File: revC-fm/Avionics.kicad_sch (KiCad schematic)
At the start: 45 parts, among them Q32 MMBT4403WT1G, SW1 KMR231NG LFS, U11 ATSAMD51N20A-AUT, U12 MR25H40MDF, U13 MAX706RESA, U4 imu-stamp-revA, Y1 32.768kHz

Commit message: working revC
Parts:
- removed D1: WS2812B, LED_SMD:LED_WS2812B_PLCC4_5.0x5.0mm_P3.2mm, symbol mainboard-rescue:WS2812B-LED-mainboard-rescue
- removed R27: R_US, Resistor_SMD:R_0603_1608Metric, symbol Device:R_US
- added C5, C6, C7: 0.1uF, Capacitor_SMD:C_0603_1608Metric, symbol Device:C
- added D1, D10, D11, D12: SK6812-EC321F, mainboard-SLI:SK6812-EC3210F, symbol mainboard_SLI:SK6812-EC321F
- R25: value R_US -> 976k
- R26: value R_US -> 102k
- R44, R46: value 4.7k -> 2.7k
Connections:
- net 3.3V: now also C5.1, C6.1, C7.1, D1.4 (VDD), D10.4 (VDD), D11.4 (VDD), D12.4 (VDD)
- net GND: now also R26.2, U4.8 (XORL1), C5.2, C6.2, C7.2, D1.1 (VSS), D10.1 (VSS), D11.1 (VSS), D12.1 (VSS)
- net NeoPixel_Out: now also D12.2 (DOUT)
- net at U11.71 (PA21): now also D1.3 (DIN)
- net AIN10 renamed BATT_NTC
- new net: D11.2 (DOUT), D12.3 (DIN)
- new net: D10.2 (DOUT), D11.3 (DIN)
- new net: D1.2 (DOUT), D10.3 (DIN)
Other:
- note added: "XOR1 = 0x0 XOR2 = 0x1"
- note added: "gyros @ 0x68, 0x69 accels @ ox4C, 0x4D mags @ 0x30, 0x31"
- note removed: "TODO: CALCULATE XOR VALUE RESISTORS FOR I2C"
- note removed: "renamed"
- moved on the sheet: C19, C20, C21, C22, C23, C24, C25, C26, C27, C28, C29, C30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

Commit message: working revC
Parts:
- added R16: 1k, Resistor_SMD:R_0603_1608Metric, symbol Device:R_US
- renumbered C31 to C10, C32 to C11, C33 to C12, C34 to C13, C36 to C14, C37 to C15, C20 to C16, C26 to C17, C28 to C18, C21 to C19, C22 to C20, C4 to C21, C5 to C22, C19 to C23, C7 to C24, C6 to C25, C35 to C26, C23 to C4, C24 to C5, C25 to C6, C27 to C7, C29 to C8, C30 to C9, D10 to D1, D1 to D2, D12 to D3, D11 to D4, R41 to R10, R51 to R11, R42 to R12, R43 to R13, R25 to R14, R5 to R15, R26 to R17, R24 to R18, R48 to R19, R50 to R20, R46 to R21, R44 to R22, R45 to R23, R47 to R8, R49 to R9, U13 to U4, U4 to U5, U11 to U6, U12 to U7
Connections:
- net at Q32.3 (C), R18.1: now also R16.1; no longer U5.5 (EN)
- new net: R16.2, U5.5 (EN)
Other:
- moved on the sheet: C21, Q32, R14, R15, R17, R18, U5

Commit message: working revC
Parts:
- removed Q32: MMBT4403WT1G, Package_TO_SOT_SMD:SOT-323_SC-70, symbol mainboard-rescue:Q_PNP_BEC-Device-mainboard-rescue
- removed R18: 10Meg, Resistor_SMD:R_0603_1608Metric, symbol Device:R_US
- added C98: 0.1uF, Capacitor_SMD:C_0603_1608Metric, symbol Device:C
- added R16, R20, R21: 1k, Resistor_SMD:R_0603_1608Metric, symbol Device:R_US
- added R26: 470k, Resistor_SMD:R_0603_1608Metric, symbol Device:R_US
- added R27: 39k, Resistor_SMD:R_0603_1608Metric, symbol Device:R_US
- D1, D2, D3, D4: value SK6812-EC321F -> SK68xx-EC3210x; footprint mainboard-SLI:SK6812-EC3210F -> SierraLobo:SK68xx-EC3210x; symbol mainboard_SLI:SK6812-EC321F -> SierraLobo:SK68xx-EC3210x
- R15: value 1Meg -> 1k
- R25: renamed from R23; value 100k -> 10k
- SW1: footprint mainboard:BTN_KMR2_4.6X2.8 -> SierraLobo:KMR2_4.6X2.8; symbol mainboard:SWITCH_SMT4.6X2.8 -> Switch:SW_SPST; Flight KMR231NG LFS -> (none); Manufacturer_Name C&K -> (none); Manufacturer_Part_Number KMR231NG LFS -> (none); Proto KMR231NG LFS -> (none)
- U4: value MAX706RESA -> MAX708RESA-T; symbol mainboard:MAX708RESA-T -> SierraLobo:MAX708RESA-T; Flight MAX706RESA -> (none); Manufacturer_Name Maxim Integrated -> (none); Manufacturer_Part_Number MAX706RESA -> (none); Proto MAX706RESA -> (none)
- U5: footprint mainboard-SLI:imu-stamp-revA-SMD -> SierraLobo:imu-stamp-revA-SMD; symbol FP-Interface-Card:imu-stamp-revA -> SierraLobo:imu-stamp-revA
- U6: symbol mainboard_SLI:ATSAMD51N20A-AUT -> SierraLobo:ATSAMD51N20A-AUT; MANUFACTURER Microchip -> (none); STANDARD IPC-7351B -> (none)
- U7: footprint mainboard:SON127P600X500X90-9N -> SierraLobo:SON127P600X500X90-9N; symbol mainboard:MR25H40MDF -> SierraLobo:MR25H40MDF; Flight MR25H40MDF -> (none); Manufacturer_Name Everspin Technologies Inc. -> (none); Manufacturer_Part_Number W25Q80DVSNIG -> (none); Proto W25Q80DVSNIG -> (none)
- Y1: Flight ABS07-32.768KHZ-T -> (none); Manufacturer_Name Abracon LLC -> (none); Manufacturer_Part_Number SC-32S32.768kHz20PPM7pF -> (none); Proto SC-32S32.768kHz20PPM7pF -> (none)
- renumbered R16 to R17, R17 to R18, R20 to R22, R21 to R23, R22 to R24
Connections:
- net +3V3 is gone; now on net 3.3V: C21.1, U5.1 (VCC)
- net ~{IMU_EN} is gone; now on an unnamed net: R15.1
- net GND: now also SW1.2 (B), C98.2, R27.1; no longer SW1.B (S), SW1.B' (S1)
- net VPYLD_PG: now reaches U6.13 (PB06)
- net VPYLD_EN: now reaches U6.14 (PB07)
- net VRF_PG: now reaches U6.36 (PB14)
- net VRF_EN: now reaches U6.37 (PB15)
- net at U6.71 (PA21): now also R16.2; no longer D2.3 (DIN)
- net at D4.2 (DOUT): now also R20.2; no longer D3.3 (DIN)
- net at D4.3 (DIN): now also R21.1; no longer D1.2 (DOUT)
- net at D1.3 (DIN): no longer D2.2 (DOUT)
- net IMU_EN: now reaches R17.1
- net at R15.2: now also D2.2 (DOUT)
- net AIN7 renamed SOLAR
- net SOLAR: now also C98.1, R26.2, R27.2
- net ~{IMU_RST}: no longer names the net of U6.83 (PC25)
- new net: R10.1, SW1.1 (A)
- new net: D1.2 (DOUT), R21.2
- new net: D3.3 (DIN), R20.1
- new net: D2.3 (DIN), R16.1
- new net VSOLAR: R26.1
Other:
- moved on the sheet: C10, C11, C12, C13, C14, C15, C16, C17, C18, C19, C20, C21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

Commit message: routing fm
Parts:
- added U36: 74HC595PW,118, Package_SO:TSSOP-16_4.4x5mm_P0.65mm, symbol SierraLobo:74HC595PW,118
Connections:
- net ~{LED_EN} is gone; now on net MUX_S0: U6.79 (PB23)
- net 3.3V: no longer C22.1, C23.1, C24.1, C25.1, D1.4 (VDD), D2.4 (VDD), D3.4 (VDD), D4.4 (VDD)
- net DAC0: no longer U6.7 (PA02)
- net ENAB_GPS: now also U6.72 (PA22); no longer U6.98 (PB01)
- net MUX_S0: no longer U6.72 (PA22)
- net RF1_CS: now also U6.98 (PB01); no longer U6.68 (PB20)
- net SD_CS: now also U6.49 (PA15); no longer U6.87 (PA27)
- net CHRG_SHDN: now reaches U6.16 (PB09)
- net PC20: now reaches U6.60 (PC20)
- net RF2_IO4: now reaches U6.61 (PC21)
- net RF2_RST: now reaches U6.82 (PC24)
- net RF2_IO0: now reaches U6.83 (PC25)
- net AIN11 renamed PC01
- net AIN4 renamed PC02
- net AIN5 renamed AMUX
- net EN_PAYLOAD renamed ENAB_RF2
- net EN_RF renamed ENAB_RF1
- net NeoPixel_Out renamed LED_OUT
- net ~{CHRG_SHDN} renamed PB21
- net ~{CHRG} renamed CHRG_STAT
- net ~{MUX_EN} renamed ~{MUX_EN1}
- new net LED_PWR: C22.1, C23.1, C24.1, C25.1, D1.4 (VDD), D2.4 (VDD), D3.4 (VDD), D4.4 (VDD)
- new net PA02: U6.7 (PA02)
- new net PA27: U6.87 (PA27)
- new net RF2_CS: U6.68 (PB20)
- no-connect marks 4 -> 1
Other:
- added sheet Temp Sensor 8 (temp_senkicad_sch.kicad_sch)
- note added: "Can also be Analog inputs"
- note added: "Place by IMU"
- moved on the sheet: C21, R14, R17, R18, U5

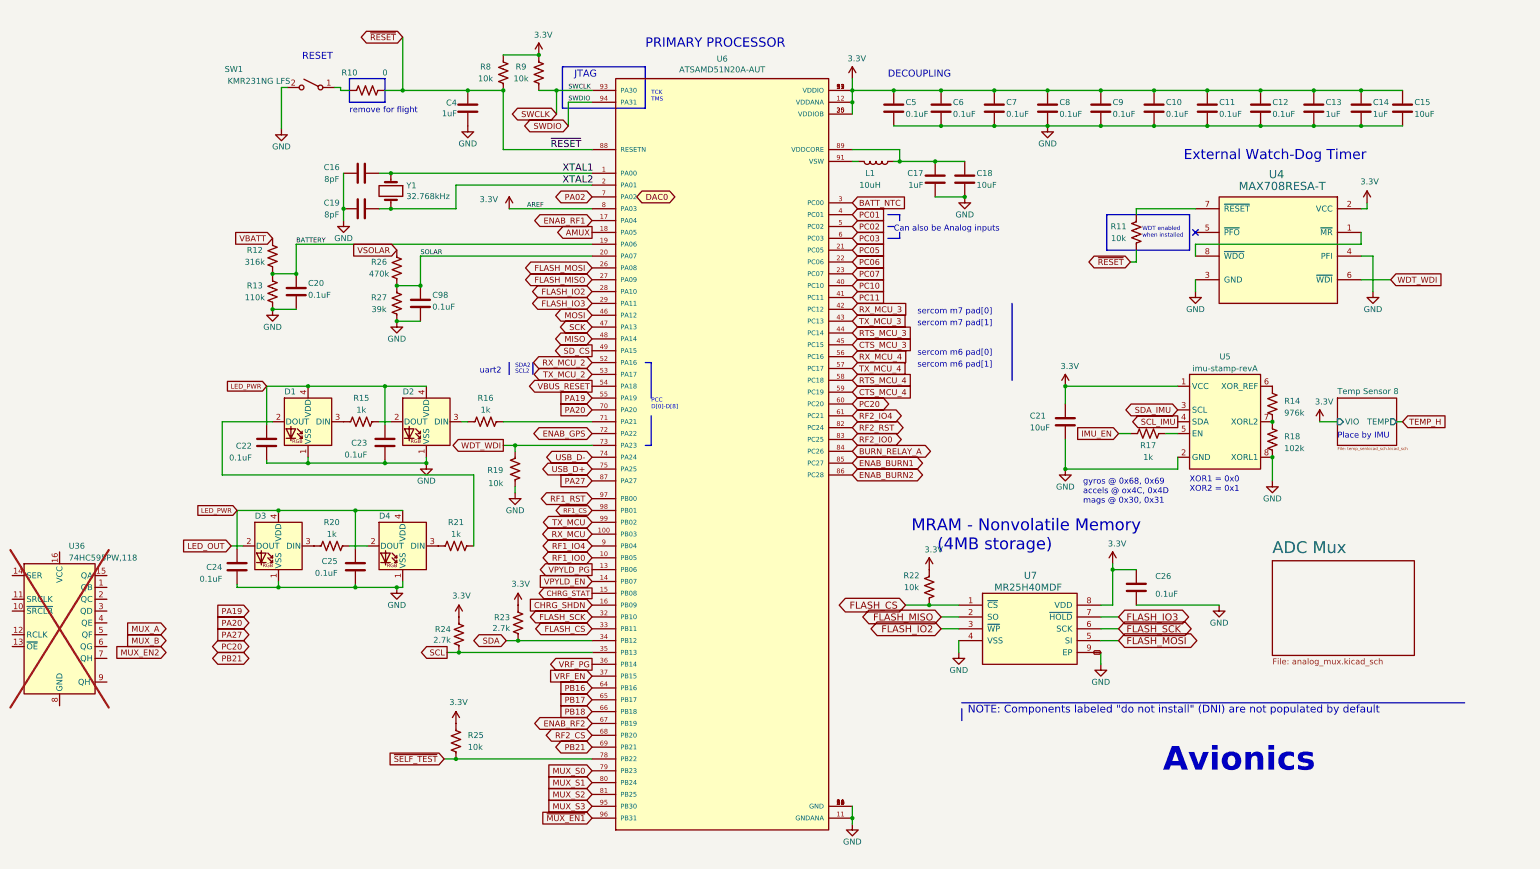
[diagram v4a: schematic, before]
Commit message: updated analog , solar comp, layout
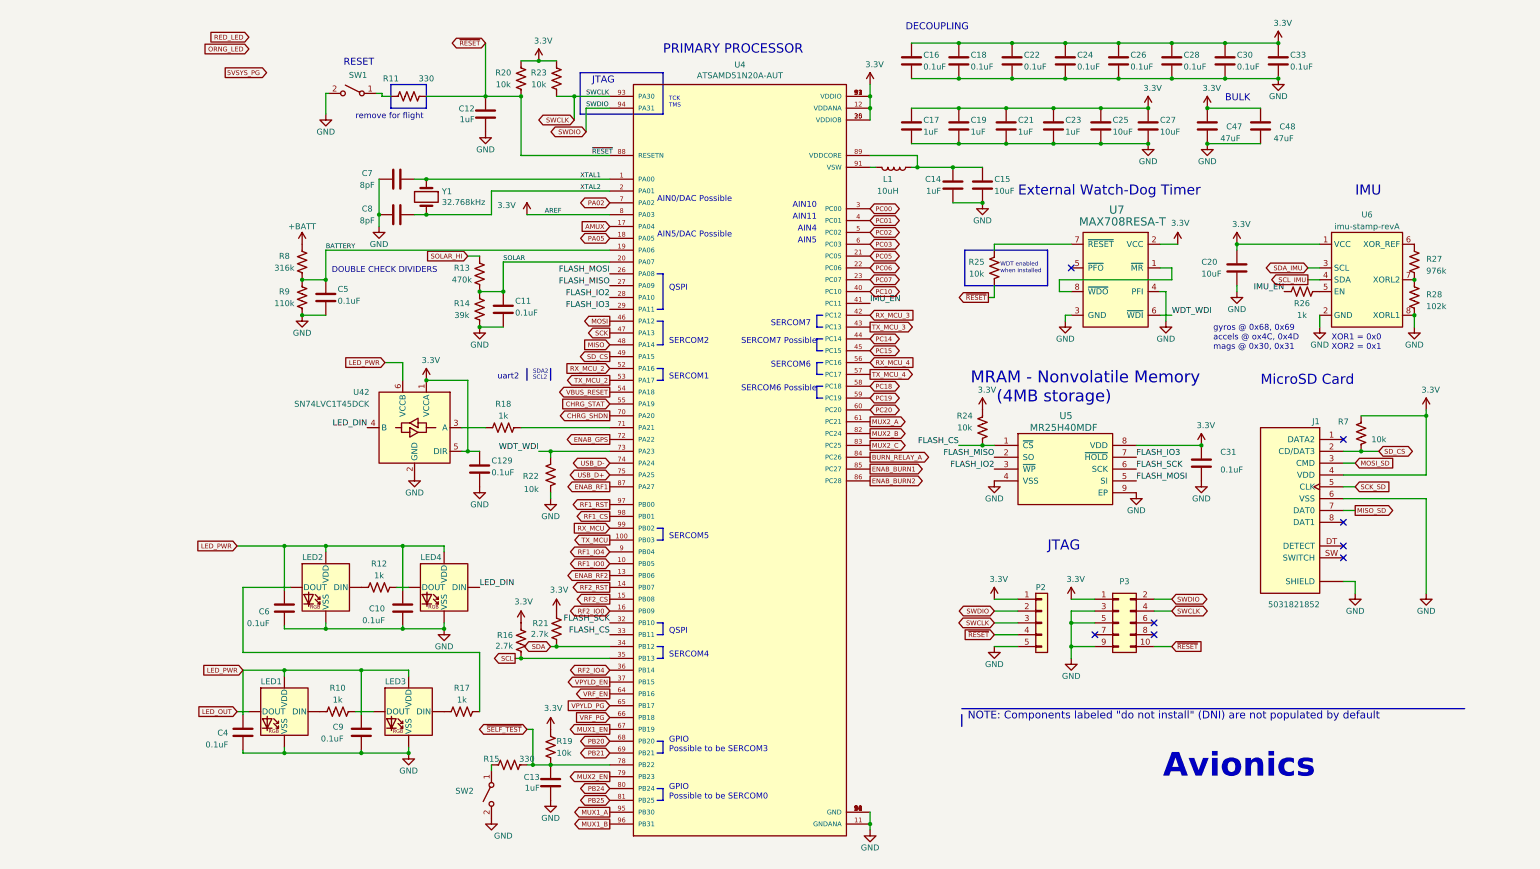
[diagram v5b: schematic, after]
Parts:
- removed U36: 74HC595PW,118, Package_SO:TSSOP-16_4.4x5mm_P0.65mm, symbol SierraLobo:74HC595PW,118
- added C129: 0.1uF, Capacitor_SMD:C_0402_1005Metric, symbol Device:C
- added C13, C21, C23: 1uF, Capacitor_SMD:C_0603_1608Metric, symbol Device:C
- added C27: 10uF, Capacitor_SMD:C_0805_2012Metric, symbol Device:C
- added C47, C48: 47uF, Capacitor_SMD:C_1206_3216Metric, symbol Device:C
- added J1: 5031821852, SierraLobo:MOLEX_503182-1852, symbol SierraLobo:503182-1852
- added P2: TSM-105-01-F-SV, Connector_PinHeader_2.54mm:PinHeader_1x05_P2.54mm_Vertical_SMD_Pin1Right, symbol Connector_Generic:Conn_01x05
- added P3: FTSH-105-01-F-DV-K-TR, Connector_PinHeader_1.27mm:PinHeader_2x05_P1.27mm_Vertical_SMD, symbol Connector_Generic:Conn_02x05_Odd_Even
- added R15: 330, Resistor_SMD:R_0603_1608Metric, symbol Device:R_US
- added R7: 10k, Resistor_SMD:R_0603_1608Metric, symbol Device:R_US
- added SW2: KMR231NG LFS, SierraLobo:KMR2_4.6X2.8, symbol Switch:SW_SPST
- added U42: SN74LVC1T45DCK, Package_TO_SOT_SMD:SOT-363_SC-70-6, symbol Logic_LevelTranslator:SN74LVC1T45DCK
- C10: renamed from C23; footprint Capacitor_SMD:C_0603_1608Metric -> Capacitor_SMD:C_0402_1005Metric
- C11: renamed from C98; footprint Capacitor_SMD:C_0603_1608Metric -> Capacitor_SMD:C_0402_1005Metric
- C16: renamed from C5; footprint Capacitor_SMD:C_0603_1608Metric -> Capacitor_SMD:C_0402_1005Metric
- C18: renamed from C6; footprint Capacitor_SMD:C_0603_1608Metric -> Capacitor_SMD:C_0402_1005Metric
- C22: renamed from C7; footprint Capacitor_SMD:C_0603_1608Metric -> Capacitor_SMD:C_0402_1005Metric
- C24: renamed from C8; footprint Capacitor_SMD:C_0603_1608Metric -> Capacitor_SMD:C_0402_1005Metric
- C26: renamed from C9; footprint Capacitor_SMD:C_0603_1608Metric -> Capacitor_SMD:C_0402_1005Metric
- C28: renamed from C10; footprint Capacitor_SMD:C_0603_1608Metric -> Capacitor_SMD:C_0402_1005Metric
- C30: renamed from C11; footprint Capacitor_SMD:C_0603_1608Metric -> Capacitor_SMD:C_0402_1005Metric
- C31: renamed from C26; footprint Capacitor_SMD:C_0603_1608Metric -> Capacitor_SMD:C_0402_1005Metric
- C33: renamed from C12; footprint Capacitor_SMD:C_0603_1608Metric -> Capacitor_SMD:C_0402_1005Metric
- C4: renamed from C24; footprint Capacitor_SMD:C_0603_1608Metric -> Capacitor_SMD:C_0402_1005Metric
- C5: renamed from C20; footprint Capacitor_SMD:C_0603_1608Metric -> Capacitor_SMD:C_0402_1005Metric
- C6: renamed from C22; footprint Capacitor_SMD:C_0603_1608Metric -> Capacitor_SMD:C_0402_1005Metric
- C7: renamed from C16; footprint Capacitor_SMD:C_0603_1608Metric -> Capacitor_SMD:C_0402_1005Metric
- C8: renamed from C19; footprint Capacitor_SMD:C_0603_1608Metric -> Capacitor_SMD:C_0402_1005Metric
- C9: renamed from C25; footprint Capacitor_SMD:C_0603_1608Metric -> Capacitor_SMD:C_0402_1005Metric
- R11: renamed from R10; value 0 -> 330
- renumbered C4 to C12, C17 to C14, C18 to C15, C13 to C17, C14 to C19, C21 to C20, C15 to C25, D3 to LED1, D1 to LED2, D4 to LED3, D2 to LED4, R20 to R10, R15 to R12, R26 to R13, R27 to R14, R24 to R16, R21 to R17, R16 to R18, R25 to R19, R8 to R20, R23 to R21, R19 to R22, R9 to R23, R22 to R24, R11 to R25, R17 to R26, R14 to R27, R18 to R28, R12 to R8, R13 to R9, U6 to U4, U7 to U5, U5 to U6, U4 to U7
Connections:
- net PA19 is gone; now on net CHRG_STAT: U4.55 (PA19)
- net PA20 is gone; now on net CHRG_SHDN: U4.70 (PA20)
- net PA27 is gone; now on net ENAB_RF1: U4.87 (PA27)
- net PB16 is gone; now on net VRF_EN: U4.64 (PB16)
- net PB17 is gone; now on net VPYLD_PG: U4.65 (PB17)
- net PB18 is gone; now on net VRF_PG: U4.66 (PB18)
- net PC11 is gone; now on net IMU_EN: U4.41 (PC11)
- net 3.3V: now also C129.1, C21.1, C23.1, C27.1, C47.1, C48.1, J1.4 (VDD), P2.1 (Pin_1), P3.1 (Pin_1), R7.2, U42.1 (VCCA), U42.5 (DIR)
- net AMUX: now also U4.17 (PA04); no longer U4.18 (PA05)
- net CHRG_SHDN: no longer U4.16 (PB09)
- net CHRG_STAT: no longer U4.15 (PB08)
- net ENAB_RF1: no longer U4.17 (PA04)
- net ENAB_RF2: now also U4.13 (PB06); no longer U4.67 (PB19)
- net GND: now also C129.2, C13.1, C21.2, C23.2, C27.2, C47.2, C48.2, J1.6 (VSS), J1.P1 (SHIELD), J1.P2 (SHIELD), J1.P3 (SHIELD), J1.P4 (SHIELD), J1.P5 (SHIELD), P2.5 (Pin_5), P3.3 (Pin_3), P3.5 (Pin_5), P3.9 (Pin_9), SW2.2 (B), U42.2 (GND)
- net LED_PWR: now also U42.6 (VCCB)
- net RF2_CS: now also U4.15 (PB08); no longer U4.68 (PB20)
- net RF2_IO0: now also U4.16 (PB09); no longer U4.83 (PC25)
- net RF2_IO4: now also U4.36 (PB14); no longer U4.61 (PC21)
- net RF2_RST: now also U4.14 (PB07); no longer U4.82 (PC24)
- net RX_MCU: now also U4.99 (PB02); no longer U4.100 (PB03)
- net SD_CS: now also J1.2 (CD/DAT3), R7.1
- net SWCLK: now also P2.3 (Pin_3), P3.4 (Pin_4)
- net SWDIO: now also P2.2 (Pin_2), P3.2 (Pin_2)
- net TX_MCU: now also U4.100 (PB03); no longer U4.99 (PB02)
- net VPYLD_EN: now also U4.37 (PB15); no longer U4.14 (PB07)
- net VPYLD_PG: no longer U4.13 (PB06)
- net VRF_EN: no longer U4.37 (PB15)
- net VRF_PG: no longer U4.36 (PB14)
- net ~{RESET}: now also P2.4 (Pin_4), P3.10 (Pin_10)
- net ~{SELF_TEST}: now also C13.2, R15.2
- net at R18.1: now also U42.3 (A); no longer LED4.3 (DIN)
- net BATT_NTC renamed PC00
- net CTS_MCU_3 renamed PC15
- net CTS_MCU_4 renamed PC19
- net MUX_S0 renamed MUX2_EN
- net MUX_S1 renamed PB24
- net MUX_S2 renamed PB25
- net MUX_S3 renamed MUX1_A
- net RTS_MCU_3 renamed PC14
- net RTS_MCU_4 renamed PC18
- net VBATT renamed +BATT
- net VSOLAR renamed SOLAR_HI
- net ~{MUX_EN1} renamed MUX1_B
- new net: R15.1, SW2.1 (A)
- new net LED_DIN: LED4.3 (DIN), U42.4 (B)
- new net MISO_SD: J1.7 (DAT0)
- new net MOSI_SD: J1.3 (CMD)
- new net MUX1_EN: U4.67 (PB19)
- new net MUX2_A: U4.61 (PC21)
- new net MUX2_B: U4.82 (PC24)
- new net MUX2_C: U4.83 (PC25)
- new net PA05: U4.18 (PA05)
- new net PB20: U4.68 (PB20)
- new net SCK_SD: J1.5 (CLK)
- no-connect marks 1 -> 8
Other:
- removed sheet ADC Mux
- removed sheet Temp Sensor 8
- note added: "AIN0/DAC Possible"
- note added: "AIN10"
- note added: "AIN11"
- note added: "AIN4"
- note added: "AIN5"
- note added: "AIN5/DAC Possible"
- note added: "BULK"
- note added: "DOUBLE CHECK DIVIDERS"
- note added: "GPIO Possible to be SERCOM0"
- note added: "GPIO Possible to be SERCOM3"
- note added: "IMU"
- note added: "MicroSD Card"
- note added: "QSPI"
- note added: "SERCOM1"
- note added: "SERCOM2"
- note added: "SERCOM4"
- note added: "SERCOM5"
- note added: "SERCOM6"
- note added: "SERCOM6 Possible"
- note added: "SERCOM7"
- note added: "SERCOM7 Possible"
- note removed: "Can also be Analog inputs"
- note removed: "PCC D[0]-D[8]"
- note removed: "Place by IMU"
- note removed: "sercom m6 pad[0]"
- note removed: "sercom m6 pad[1]"
- note removed: "sercom m7 pad[0]"
- note removed: "sercom m7 pad[1]"
- moved on the sheet: C10, C11, C12, C14, C15, C16, C17, C18, C19, C20, C22, C24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

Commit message: routing
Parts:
- added R271: 1k, Resistor_SMD:R_0603_1608Metric, symbol Device:R_US
- C10: renamed from C30; footprint Capacitor_SMD:C_0402_1005Metric -> Capacitor_SMD:C_0603_1608Metric
- C11: renamed from C33; footprint Capacitor_SMD:C_0402_1005Metric -> Capacitor_SMD:C_0603_1608Metric
- C26: renamed from C5; footprint Capacitor_SMD:C_0402_1005Metric -> Capacitor_SMD:C_0603_1608Metric
- C27: renamed from C11; footprint Capacitor_SMD:C_0402_1005Metric -> Capacitor_SMD:C_0603_1608Metric
- C28: renamed from C31; footprint Capacitor_SMD:C_0402_1005Metric -> Capacitor_SMD:C_0603_1608Metric
- C29: renamed from C129; footprint Capacitor_SMD:C_0402_1005Metric -> Capacitor_SMD:C_0603_1608Metric
- C30: renamed from C6; footprint Capacitor_SMD:C_0402_1005Metric -> Capacitor_SMD:C_0603_1608Metric
- C31: renamed from C10; footprint Capacitor_SMD:C_0402_1005Metric -> Capacitor_SMD:C_0603_1608Metric
- C32: renamed from C4; footprint Capacitor_SMD:C_0402_1005Metric -> Capacitor_SMD:C_0603_1608Metric
- C33: renamed from C9; footprint Capacitor_SMD:C_0402_1005Metric -> Capacitor_SMD:C_0603_1608Metric
- C4: renamed from C16; footprint Capacitor_SMD:C_0402_1005Metric -> Capacitor_SMD:C_0603_1608Metric
- C5: renamed from C18; footprint Capacitor_SMD:C_0402_1005Metric -> Capacitor_SMD:C_0603_1608Metric
- C6: renamed from C22; footprint Capacitor_SMD:C_0402_1005Metric -> Capacitor_SMD:C_0603_1608Metric
- C7: renamed from C24; footprint Capacitor_SMD:C_0402_1005Metric -> Capacitor_SMD:C_0603_1608Metric
- C8: renamed from C26; footprint Capacitor_SMD:C_0402_1005Metric -> Capacitor_SMD:C_0603_1608Metric
- C9: renamed from C28; footprint Capacitor_SMD:C_0402_1005Metric -> Capacitor_SMD:C_0603_1608Metric
- renumbered C17 to C13, C19 to C14, C21 to C15, C23 to C16, C25 to C17, C27 to C18, C7 to C21, C14 to C22, C15 to C23, C8 to C24, C20 to C25, C13 to C34, LED2 to LED1, LED4 to LED2, LED1 to LED3, LED3 to LED4, R8 to R10, R27 to R11, R25 to R12, R26 to R14, R9 to R15, R28 to R16, R14 to R17, R24 to R19, R7 to R20, R22 to R21, R12 to R22, R21 to R23, R16 to R24, R10 to R25, R17 to R26, R19 to R27, R15 to R28, R20 to R7, R23 to R8, R11 to R9, U7 to U4, U6 to U5, U42 to U6, U5 to U7, U4 to U8
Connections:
- net LED_DIN: now also R271.2; no longer LED2.3 (DIN)
- net PB20 renamed ~{5VPYLD_ALERT}
- net PB21 renamed ~{5VSYS_ALERT}
- net VPYLD_EN renamed 5VSYS_EN
- net VPYLD_PG renamed 5VSYS_LATCH
- net VRF_EN renamed 5VPL_EN
- net VRF_PG renamed 5VPL_LATCH
- new net: LED2.3 (DIN), R271.1
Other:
- moved on the sheet: C34, R27, R28, SW2

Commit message: fm layout
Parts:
- LED1, LED2, LED3, LED4: footprint SierraLobo:SK68xx-EC3210x -> SierraLobo:LED_SK68xx-EC3210x
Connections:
- net RX_MCU: now also U8.100 (PB03); no longer U8.99 (PB02)
- net TX_MCU: now also U8.99 (PB02); no longer U8.100 (PB03)
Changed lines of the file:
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@@
     )
   )
-  (global_label "TX_MCU" (shape output) (at 104.14 124.46 180) (fields_autoplaced)
+  (global_label "TX_MCU" (shape output) (at 104.14 121.92 180) (fields_autoplaced)
     (effects (font (size 1.016 1.016)) (justify right))
-    (property "Intersheetrefs" "${INTERSHEET_REFS}" (at 94.6918 124.46 0)
+    (property "Intersheetrefs" "${INTERSHEET_REFS}" (at 94.6918 121.92 0)
       (effects (font (size 1.016 1.016)) (justify right) hide)
     )
@@
     )
   )
-  (global_label "RX_MCU" (shape input) (at 104.14 121.92 180) (fields_autoplaced)
+  (global_label "RX_MCU" (shape input) (at 104.14 124.46 180) (fields_autoplaced)
     (effects (font (size 1.016 1.016)) (justify right))
-    (property "Intersheetrefs" "${INTERSHEET_REFS}" (at 94.3894 121.92 0)
+    (property "Intersheetrefs" "${INTERSHEET_REFS}" (at 94.3894 124.46 0)
       (effects (font (size 1.016 1.016)) (justify right) hide)
     )
@@
       (effects (font (size 1.27 1.27)) (justify left top) hide)
     )
-    (property "Footprint" "SierraLobo:SK68xx-EC3210x" (at 59.69 168.91 0)
+    (property "Footprint" "SierraLobo:LED_SK68xx-EC3210x" (at 59.69 168.91 0)
       (effects (font (size 1.27 1.27)) (justify left top) hide)
     )
@@
       (effects (font (size 1.27 1.27)) (justify left top) hide)
     )
-    (property "Footprint" "SierraLobo:SK68xx-EC3210x" (at 41.91 142.24 0)
+    (property "Footprint" "SierraLobo:LED_SK68xx-EC3210x" (at 41.91 142.24 0)
       (effects (font (size 1.27 1.27)) (justify left top) hide)
     )
@@
       (effects (font (size 1.27 1.27)) (justify left top) hide)
     )
-    (property "Footprint" "SierraLobo:SK68xx-EC3210x" (at 33.02 168.91 0)
+    (property "Footprint" "SierraLobo:LED_SK68xx-EC3210x" (at 33.02 168.91 0)
       (effects (font (size 1.27 1.27)) (justify left top) hide)
     )
@@
       (effects (font (size 1.27 1.27)) (justify left top) hide)
     )
-    (property "Footprint" "SierraLobo:SK68xx-EC3210x" (at 67.31 142.24 0)
+    (property "Footprint" "SierraLobo:LED_SK68xx-EC3210x" (at 67.31 142.24 0)
       (effects (font (size 1.27 1.27)) (justify left top) hide)
     )
